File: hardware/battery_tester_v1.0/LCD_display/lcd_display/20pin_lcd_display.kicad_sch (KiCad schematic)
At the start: 44 parts, among them J1 LED, U1 74AHCT244, U2 74AHCT244, U3 74HC595

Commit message: update lcd pcb
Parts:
- removed C?: 470u/10V, Capacitor_THT:CP_Radial_D8.0mm_P3.80mm, symbol Device:C_Polarized
- removed J?: LCD_CONN, Connector_JST:JST_XA_B05B-XASK-1_1x05_P2.50mm_Vertical, symbol Connector_Generic:Conn_01x05
- removed R6: 0R, Resistor_SMD:R_1206_3216Metric, symbol Device:R
- removed R? (x2): R, Resistor_SMD:R_0805_2012Metric_Pad1.20x1.40mm_HandSolder, symbol Device:R
- removed U2: 74AHCT244, symbol 74xx:74AHCT244
- added C1: 4u7, Capacitor_SMD:C_0805_2012Metric_Pad1.18x1.45mm_HandSolder, symbol Device:C
- added C10: 470n, Capacitor_SMD:C_0805_2012Metric_Pad1.18x1.45mm_HandSolder, symbol Device:C
- added C5: 100u/10V, Capacitor_THT:CP_Radial_D8.0mm_P3.80mm, symbol Device:C_Polarized
- added D1, D2, D3, D4, D5, D6, D7, D8, D9: LL4148, Diode_SMD:D_MiniMELF, symbol Diode:LL4148
- added J1: VCC_5V, Connector_JST:JST_XA_B02B-XASK-1_1x02_P2.50mm_Vertical, symbol Connector_Generic:Conn_01x02
- added R13: 0R, Resistor_SMD:R_0805_2012Metric_Pad1.20x1.40mm_HandSolder, symbol Device:R
- added R21: 10k, Resistor_SMD:R_0805_2012Metric_Pad1.20x1.40mm_HandSolder, symbol Device:R
- added SW1, SW2, SW3, SW4, SW5, SW6, SW7, SW8, SW9: SW_Push, My-Footprints:SW_PUSH_6mm, symbol Switch:SW_Push
- added U2: 74HCT125, Package_SO:SO-14_3.9x8.65mm_P1.27mm, symbol My-Lib:74HCT125
- LCD1: footprint (none) -> My-Footprints-displays:RG12864B_FULL
- R1: value 4k7 -> 10k; footprint Resistor_SMD:R_1206_3216Metric -> Resistor_SMD:R_0805_2012Metric_Pad1.20x1.40mm_HandSolder
- R10: renamed from R9; footprint Resistor_SMD:R_1206_3216Metric -> Resistor_SMD:R_0805_2012Metric_Pad1.20x1.40mm_HandSolder
- R11: renamed from R8; footprint Resistor_SMD:R_1206_3216Metric -> Resistor_SMD:R_0805_2012Metric_Pad1.20x1.40mm_HandSolder
- R12: renamed from R7; footprint Resistor_SMD:R_1206_3216Metric -> Resistor_SMD:R_0805_2012Metric_Pad1.20x1.40mm_HandSolder
- R14: renamed from R5; footprint Resistor_SMD:R_1206_3216Metric -> Resistor_SMD:R_0805_2012Metric_Pad1.20x1.40mm_HandSolder
- R15: renamed from R4; footprint Resistor_SMD:R_1206_3216Metric -> Resistor_SMD:R_0805_2012Metric_Pad1.20x1.40mm_HandSolder
- R16: renamed from R3; footprint Resistor_SMD:R_1206_3216Metric -> Resistor_SMD:R_0805_2012Metric_Pad1.20x1.40mm_HandSolder
- R17, R18: renamed from R?; footprint Resistor_SMD:R_0805_2012Metric -> Resistor_SMD:R_0805_2012Metric_Pad1.20x1.40mm_HandSolder
- R2: footprint Resistor_SMD:R_1206_3216Metric -> Resistor_SMD:R_0805_2012Metric_Pad1.20x1.40mm_HandSolder
- R3: renamed from R16; footprint Resistor_SMD:R_1206_3216Metric -> Resistor_SMD:R_0805_2012Metric_Pad1.20x1.40mm_HandSolder
- R4: renamed from R15; footprint Resistor_SMD:R_1206_3216Metric -> Resistor_SMD:R_0805_2012Metric_Pad1.20x1.40mm_HandSolder
- R5: renamed from R14; footprint Resistor_SMD:R_1206_3216Metric -> Resistor_SMD:R_0805_2012Metric_Pad1.20x1.40mm_HandSolder
- R6: renamed from R13; footprint Resistor_SMD:R_1206_3216Metric -> Resistor_SMD:R_0805_2012Metric_Pad1.20x1.40mm_HandSolder
- R7: renamed from R12; footprint Resistor_SMD:R_1206_3216Metric -> Resistor_SMD:R_0805_2012Metric_Pad1.20x1.40mm_HandSolder
- R8: renamed from R11; footprint Resistor_SMD:R_1206_3216Metric -> Resistor_SMD:R_0805_2012Metric_Pad1.20x1.40mm_HandSolder
- R9: renamed from R10; footprint Resistor_SMD:R_1206_3216Metric -> Resistor_SMD:R_0805_2012Metric_Pad1.20x1.40mm_HandSolder
- RV1: renamed from RV?; value 10k -> 1k
- U1: footprint (none) -> Package_SO:SO-20_5.3x12.6mm_P1.27mm
- gave numbers to parts that had none: 12
- renumbered C2 to C3, C3 to C6, C1 to C7, C4 to C9, J1 to J3, U3 to U4
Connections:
- net ~{RST}_IN is gone; now on net LATCH: J3.1 (Pin_1)
- net +5V: now also R1.1, C1.1, C5.1, J1.2 (Pin_2), R21.1, U2.14 (VCC); no longer J3.10 (Pin_10), J3.9 (Pin_9), RV1.3
- net BACKLIGHT_DRIVE: now also U4.4 (QE); no longer U4.5 (QF)
- net BACKLIGHT_DRIVE_IN: now also R13.1; no longer J3.5 (Pin_5)
- net CLK: now also J3.2 (Pin_2), R14.2, U2.5 (2A)
- net CS1: now also U4.3 (QD), U2.8 (3Y); no longer U4.4 (QE)
- net CS1_IN: now also U2.9 (3A)
- net CS2: now also U4.2 (QC), U2.11 (4Y); no longer U4.3 (QD)
- net CS2_IN: now also J2.8 (Pin_8), U2.12 (4A); no longer J2.7 (Pin_7)
- net DATA: now also J3.4 (Pin_4), R13.2
- net DB5_IN: now also J2.7 (Pin_7); no longer J2.8 (Pin_8)
- net DI: now also U2.6 (2Y)
- net EN: now also U2.3 (1Y); no longer U4.15 (QA)
- net EN_IN: now also J3.3 (Pin_3), U2.2 (1A); no longer J3.4 (Pin_4)
- net GND: now also LCD1.15 (R/~{W}), C1.2, C10.2, C5.2, J1.1 (Pin_1), U2.1 (1~{OE}), U2.10 (3~{OE}), U2.13 (4~{OE}), U2.4 (2~{OE}), U2.7 (GND); no longer J3.6 (Pin_6), J3.7 (Pin_7), J3.8 (Pin_8), R1.2
- net at RV1.1: now also R2.1; no longer LCD1.18 (VEE)
- removed net DI_IN: J3.3 (Pin_3), R14.2
- removed net RW: LCD1.15 (R/~{W}), R1.1, R2.2
- removed net RW_IN: J3.2 (Pin_2), R2.1
- net ~{RST}: no longer names the net of LCD1.14 (~{RST})
- net ~{RST}: now also C10.1, R21.2; no longer U4.2 (QC)
- new net: D4.2 (A), SW4.2
- new net: R1.2, RV1.3
- new net: D6.2 (A), SW6.2
- new net: D2.2 (A), SW2.2
- new net: LCD1.18 (VEE), R2.2
- new net: D7.2 (A), SW7.2
- new net: D5.2 (A), SW5.2
- new net: D8.2 (A), SW8.2
- new net: D9.2 (A), SW9.2
- new net: D3.2 (A), SW3.2
- new net: D1.2 (A), SW1.2
- new net COL1: J3.5 (Pin_5), SW1.1, SW2.1, SW3.1
- new net COL2: J3.6 (Pin_6), SW4.1, SW5.1, SW6.1
- new net COL3: J3.7 (Pin_7), SW7.1, SW8.1, SW9.1
- new net ROW1: D1.1 (K), D4.1 (K), D7.1 (K), J3.8 (Pin_8)
- new net ROW2: D2.1 (K), D5.1 (K), D8.1 (K), J3.9 (Pin_9)
- new net ROW3: D3.1 (K), D6.1 (K), D9.1 (K), J3.10 (Pin_10)
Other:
- note added: "PUSH BUTTONS"
- moved on the sheet: RV1

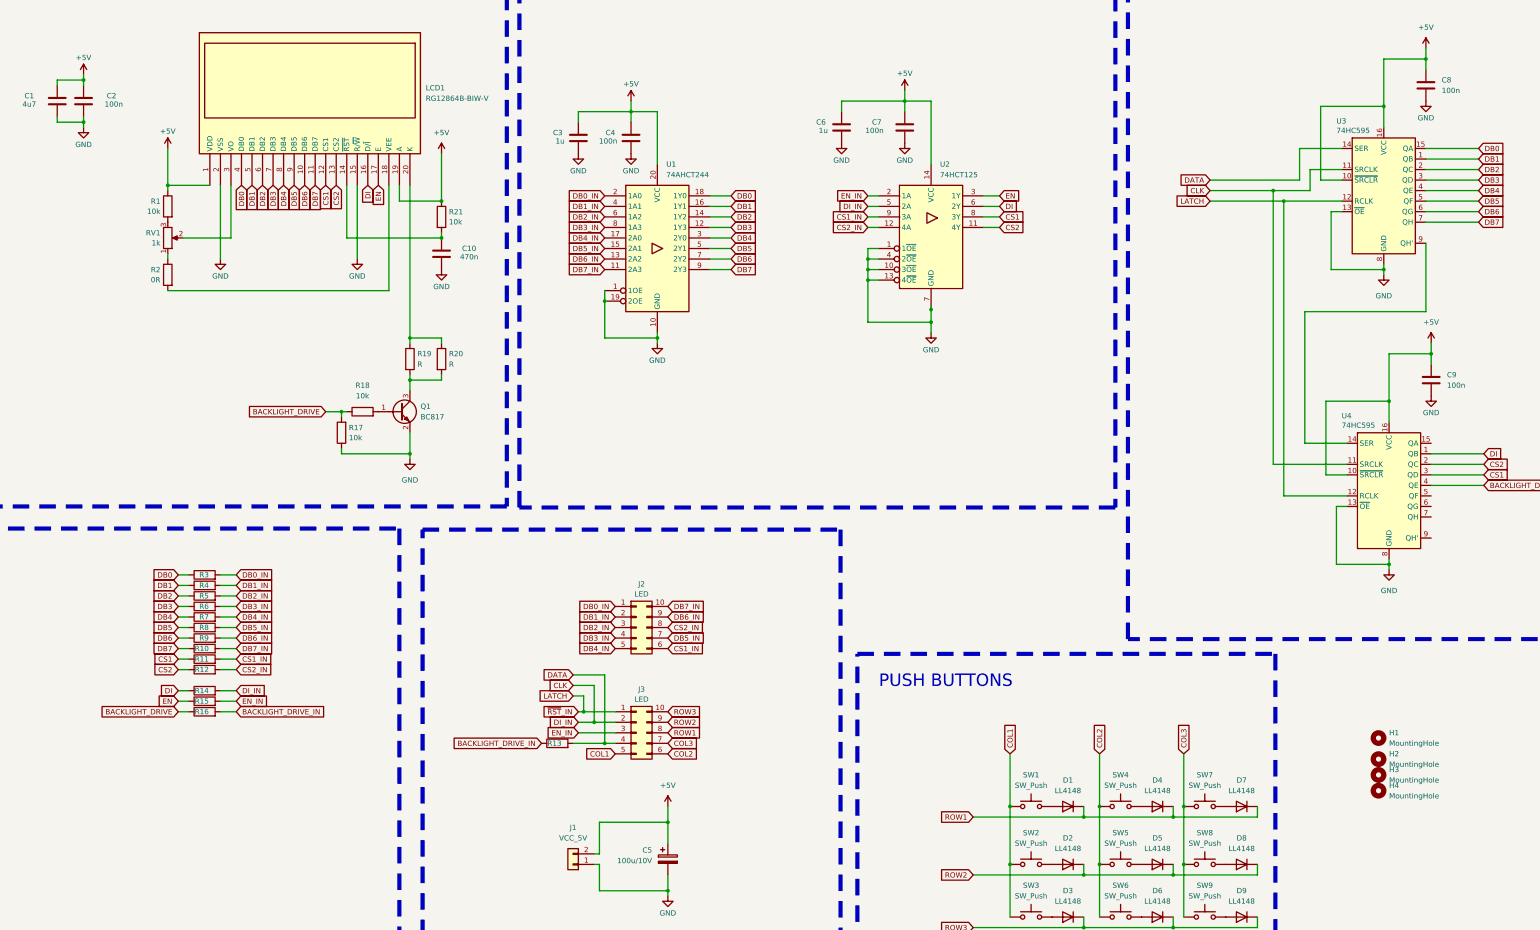
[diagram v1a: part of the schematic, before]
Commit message: update lcd display + button pcb
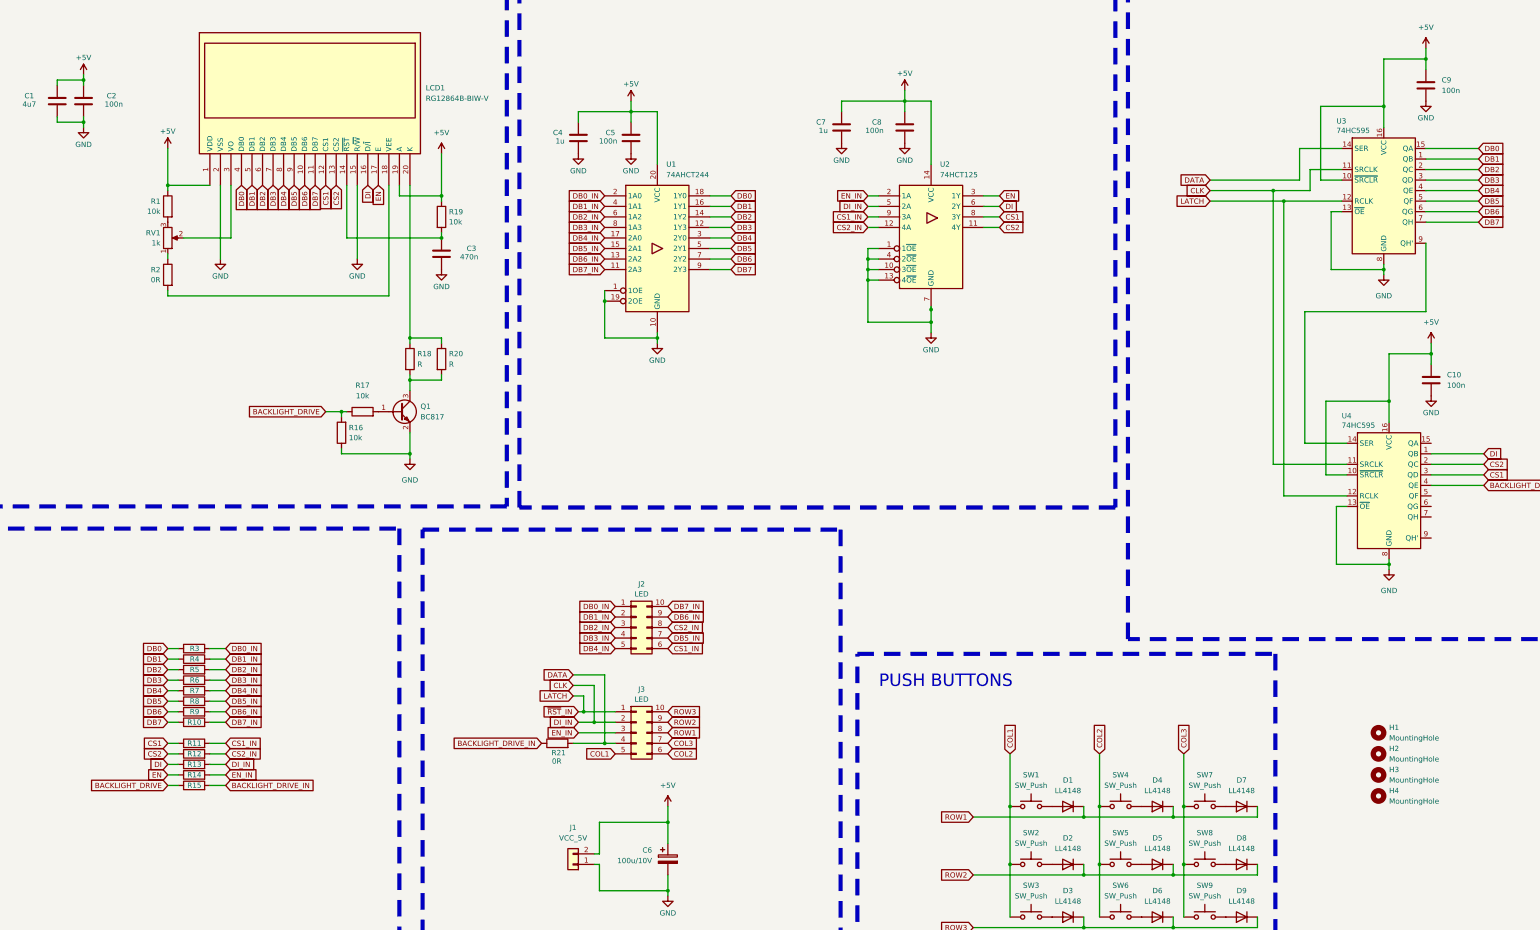
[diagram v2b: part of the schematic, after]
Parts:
- U1: footprint Package_SO:SO-20_5.3x12.6mm_P1.27mm -> Package_SO:SOIC-20W_7.5x12.8mm_P1.27mm
- renumbered C9 to C10, C10 to C3, C3 to C4, C4 to C5, C5 to C6, C6 to C7, C7 to C8, C8 to C9, R14 to R13, R15 to R14, R16 to R15, R17 to R16, R18 to R17, R19 to R18, R21 to R19, R13 to R21
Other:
- moved on the sheet: H1, H2, H4, R10, R11, R12, R13, R14, R15, R3, R4, R5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

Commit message: lcd pcb done
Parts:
- added D10, D11, D12: LED, LED_THT:LED_D5.0mm, symbol Device:LED
- added Q2, Q3, Q4: BC817, Package_TO_SOT_SMD:SOT-23, symbol Transistor_BJT:BC817
- added R22, R23, R26: 10k, Resistor_SMD:R_0805_2012Metric_Pad1.20x1.40mm_HandSolder, symbol Device:R
- added R24, R25, R27: 220R, Resistor_SMD:R_0805_2012Metric_Pad1.20x1.40mm_HandSolder, symbol Device:R
- R16: value 10k -> 100k
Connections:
- net +5V: now also D10.2 (A), D11.2 (A), D12.2 (A)
- net GND: now also Q2.2 (E), Q3.2 (E), Q4.2 (E)
- net LED1: now reaches U4.5 (QF)
- net LED1: now also R23.1
- net LED2: now reaches U4.6 (QG)
- net LED2: now also R22.1
- net LED3: now reaches U4.7 (QH)
- net LED3: now also R26.1
- new net: Q3.1 (B), R22.2
- new net: Q3.3 (C), R25.1
- new net: D10.1 (K), R24.2
- new net: Q2.1 (B), R23.2
- new net: Q2.3 (C), R24.1
- new net: D11.1 (K), R25.2
- new net: Q4.1 (B), R26.2
- new net: Q4.3 (C), R27.1
- new net: D12.1 (K), R27.2
